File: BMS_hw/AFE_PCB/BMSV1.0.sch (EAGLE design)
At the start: 250 parts, among them IC1 MC33771BEP, IC2 SFH6156, IC3 MIC28515V1, IC4 FOD8384-COC, IC5 FOD8384-COC, IC6 FOD8384-COC, Q1 IRLML5203, Q2 IRLML5203, T1 IPT020N10N3V1, T2 IPT020N10N3V1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

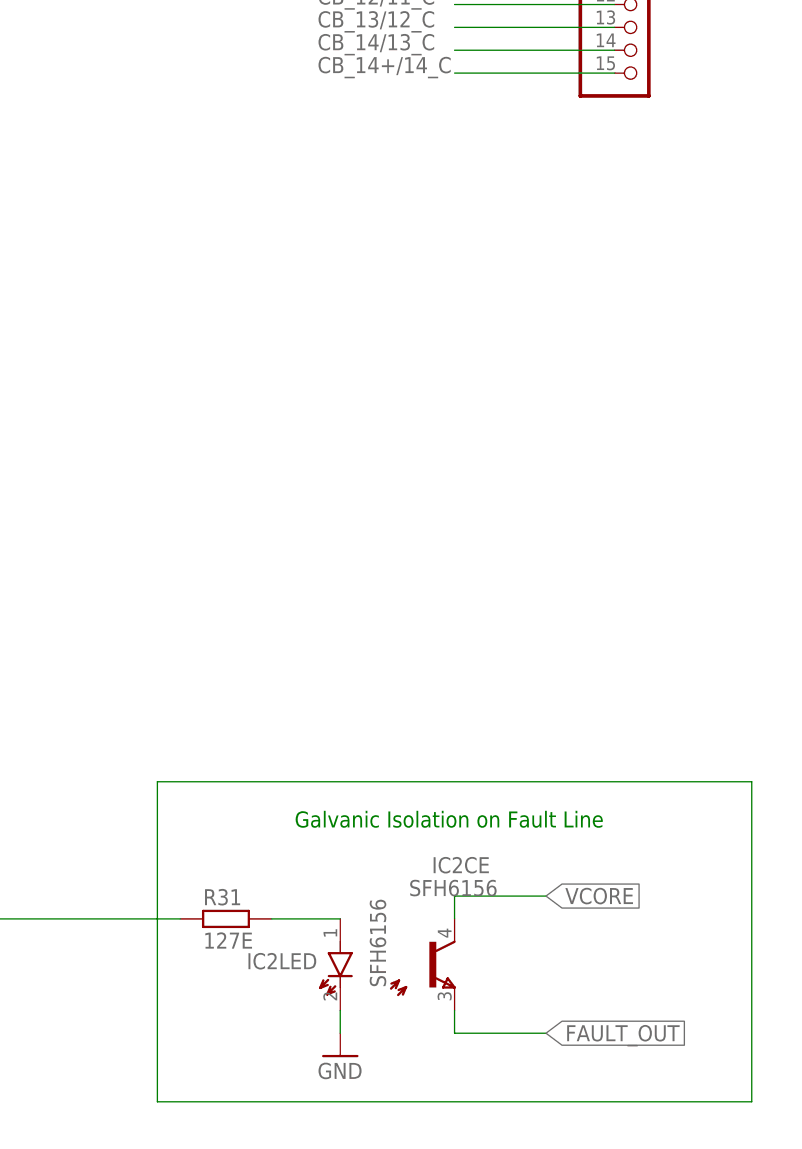
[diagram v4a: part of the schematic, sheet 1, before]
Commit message: itt @ coil-craft MSS library created, @afe layout 90% complete ! @schhematic altr @3!
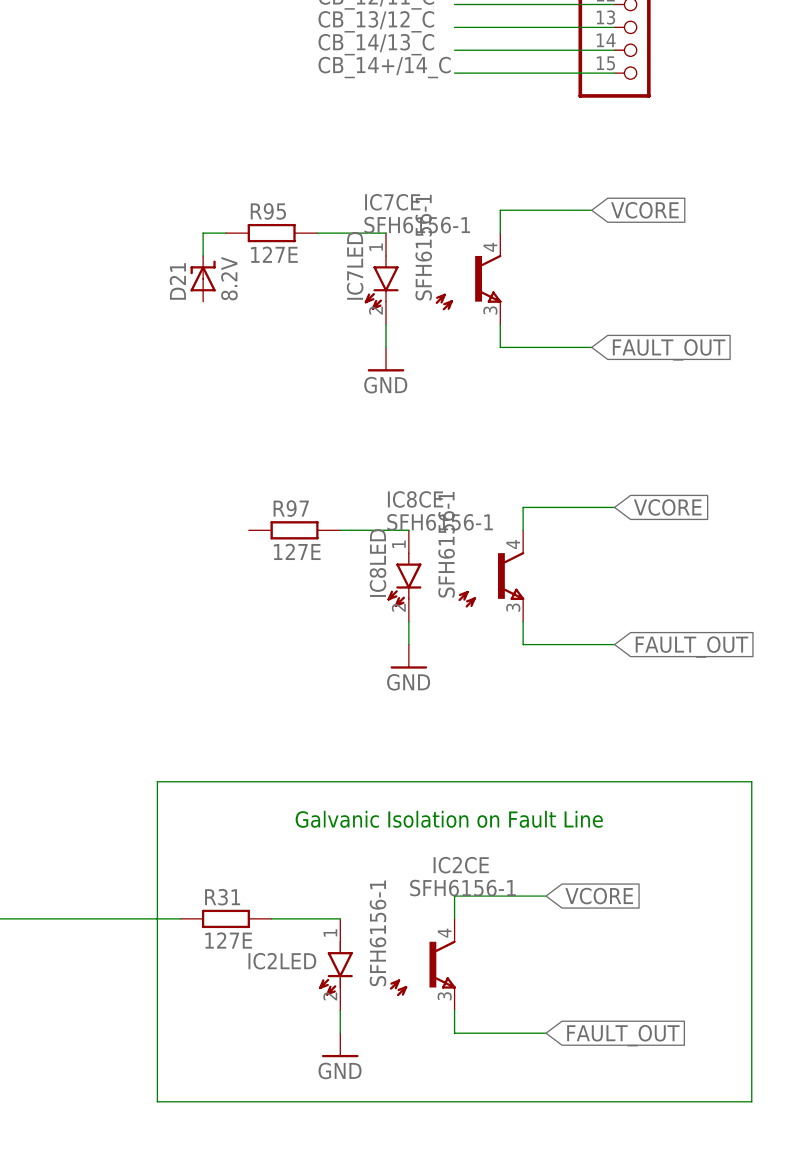
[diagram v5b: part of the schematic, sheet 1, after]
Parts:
- added D21: 8.2V, ipc-7351-diode:ZENER_SOD-123
- added IC7, IC8: SFH6156-1, optocoupler:SFH6156
- added R95, R97: 127E, ipc-7351-resistor:RESISTOR_0402
- D2: value 27V -> 33V
- IC2: value SFH6156 -> SFH6156-1
- L1: value XAL1010-822MEB -> MSS1278-D; device GreenFuel:XAL1010-822MEB -> GreenFuel:MSS1278-D
- PACK-: value (none) -> PACK-
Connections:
- new net N$25: IC7LED.A, R95.2
- new net N$27: IC8LED.A, R97.2
- new net N$36: D21.K, R95.1
- net FAULT_OUT: now also IC7CE.E, IC8CE.E
- net GND: now also IC7LED.K, IC8LED.K
- net VCORE: now also IC7CE.C, IC8CE.C

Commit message: board afe and layout
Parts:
- removed C69: 47nF, ipc-7351-capacitor:CAPACITOR_0603
- removed C70: 47nF, ipc-7351-capacitor:CAPACITOR_1210
- added C80: 2.2uF 100V, ipc-7351-capacitor:CAPACITOR_1210
- C63: value (none) -> 0.1uF 100V; device ipc-7351-capacitor:POLARISED_CASE_E -> ipc-7351-capacitor:CAPACITOR_0603
- C64: value 47nF -> 2.2uF 100V
- C65: value 47nF -> 0.1uF 100V; device ipc-7351-capacitor:CAPACITOR_0402 -> ipc-7351-capacitor:CAPACITOR_0603
- C66, C73, C74, C76, C77: device ipc-7351-capacitor:CAPACITOR_0402 -> ipc-7351-capacitor:CAPACITOR_0603
- R79, R85, R89, R90, R91: device ipc-7351-resistor:RESISTOR_0402 -> ipc-7351-resistor:RESISTOR_0603
- R80, R82: value 127E -> 1.6k; device ipc-7351-resistor:RESISTOR_0402 -> ipc-7351-resistor:RESISTOR_0603
- R83: value 127E -> 16.2k; device ipc-7351-resistor:RESISTOR_0402 -> ipc-7351-resistor:RESISTOR_0603
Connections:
- net +15V: no longer C69.1, C70.1
- net CB_10/9_C: now also JP5.4; no longer JP5.10
- net CB_12/11_C: now also JP5.5; no longer JP5.12
- net CB_13/12_C: now also JP5.10; no longer JP5.13
- net CB_14+/14_C: now also JP5.9; no longer JP5.15
- net CB_14/13_C: now also JP5.6; no longer JP5.14
- net CB_2/1_C: now also JP5.7; no longer JP5.2
- net CB_3/2_C: now also JP5.15; no longer JP5.3
- net CB_4/3_C: now also JP5.1; no longer JP5.4
- net CB_5/4_C: now also JP5.14; no longer JP5.5
- net CB_6/5_C: now also JP5.2; no longer JP5.6
- net CB_7/6_C: now also JP5.13; no longer JP5.7
- net CB_8/7_C: now also JP5.3; no longer JP5.8
- net CB_9/8_C: now also JP5.12; no longer JP5.9
- net CELL1-: now also JP5.8; no longer JP5.1
- net GND: now also C63.1, C64.1, C80.1; no longer C63.-, C64.2, C69.2, C70.2
- net N$29: now also C63.2, C64.2, C80.2; no longer C63.+, C64.1
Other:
- moved on the sheet: C48, C49, C50, C51, C52, C53, C54, C55, C56, C57, C58, C59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

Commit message: itt@8
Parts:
- added R107: (no value), ipc-7351-resistor:RESISTOR_0603
- PACK-: value PACK- -> (none)
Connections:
- removed net FAULT: X2-5.S
- new net N$12: IC3.EN, R107.1
- net CSB: now also X3-7.S
- net FAULT_OUT: now also X2-5.S
- net GND: now also IC3.MODE; no longer X3-7.S
- net VIN: now also R107.2
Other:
- moved on the sheet: C48, C63, C64, C65, C66, C73, C74, C76, C77, C80, IC3, L1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

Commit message: @ITT9
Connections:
- removed net ISP: X2-11.S
- net GND: no longer X2-1.S, X2-6.S
- net MISO: now also X2-11.S
- net MOSI: now also X2-6.S
- net SCLK: now also X2-1.S
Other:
- moved on the sheet: R6
